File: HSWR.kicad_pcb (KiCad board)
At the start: 4 copper layers, 152 x 139 mm, 159 parts, among them IC1 B1212S-2W, IC3 JW5052C, IC4 ADM3054, IC5 ADuM4160, J1 USB_B, J2 IO, J3 B+, J4 B-, J5 U, J6 V, J7 W, J8 SWD, J9 AVR-ISP-6, Q1 IXFK300N20X3, Q2 IXFK300N20X3, Q3 IXFK300N20X3, Q4 IXFK300N20X3, Q5 IXFK300N20X3, Q6 IXFK300N20X3, Q7 Q_NMOS_GDS, U1 ACS781xLRTR-150B, U10 AM26LV32xD, U11 ADuM120N1, U12 ADuM120N1, U13 PC355, U2 ACS781xLRTR-150B, U3 ACS781xLRTR-150B, U4 STM32F405RGTx, U5 IRS2186, U6 IRS2186, U7 IRS2186, U8 AP1117-50, U9 ATtiny13A-SU, Y1 8MHz

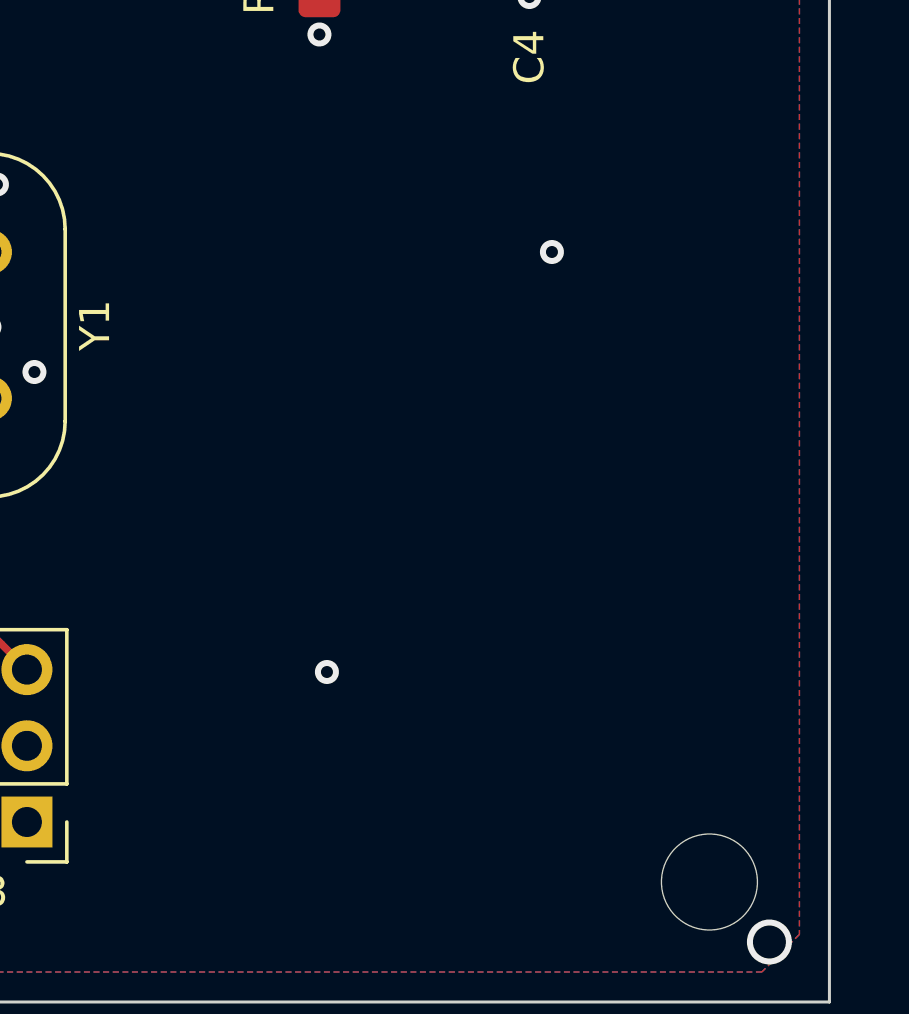
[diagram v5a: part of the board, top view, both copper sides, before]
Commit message: - added sponsor logo
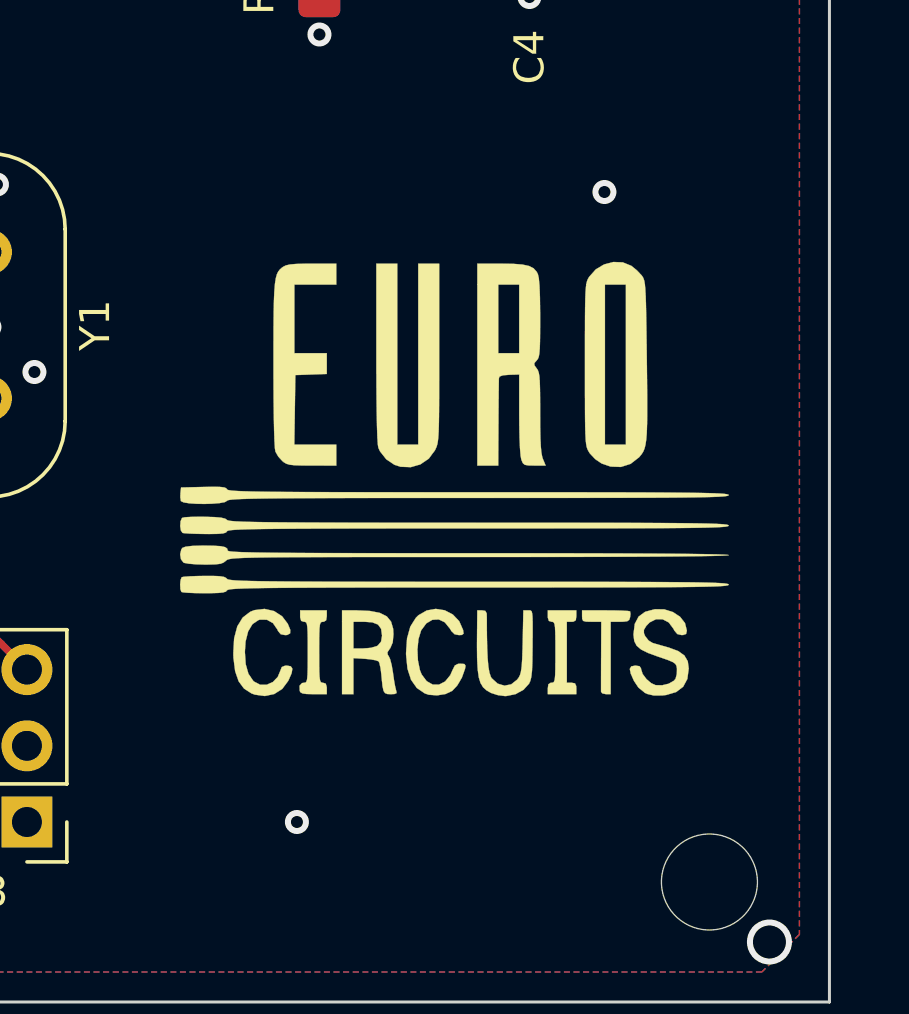
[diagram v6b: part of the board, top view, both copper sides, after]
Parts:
- added G***: LOGO, HSWR:Eurocircuits Logo, F.Cu at (206.5, 145.5)
